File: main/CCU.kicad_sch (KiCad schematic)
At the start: 8 parts, among them U2 ESP32-DevKitC, U27 Oak-D, U4 Waveshare 23721, U5 MPU6050

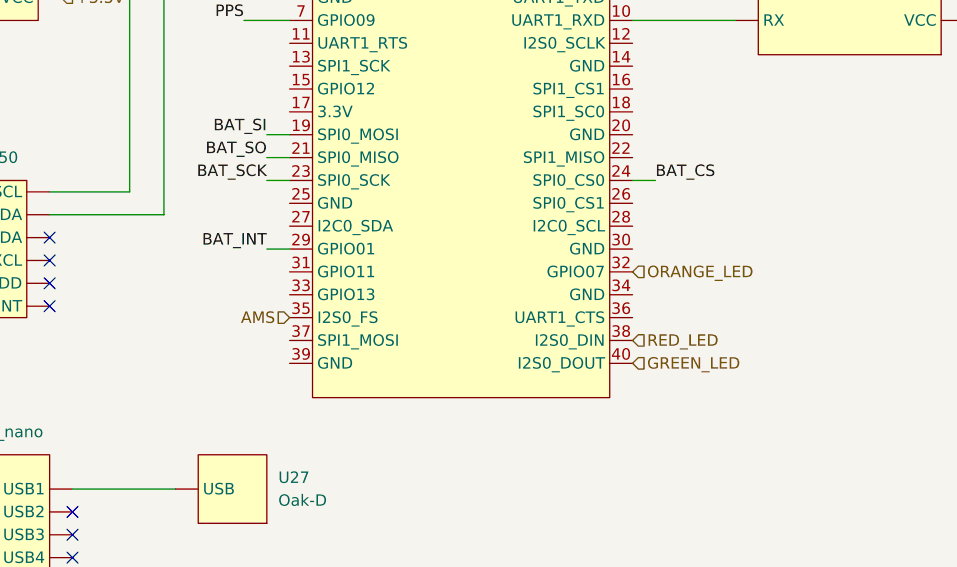
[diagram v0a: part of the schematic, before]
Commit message: added nwe sheet (switching system), created a few new symbols, changed +48V coming from battery to Battery_High_voltage,
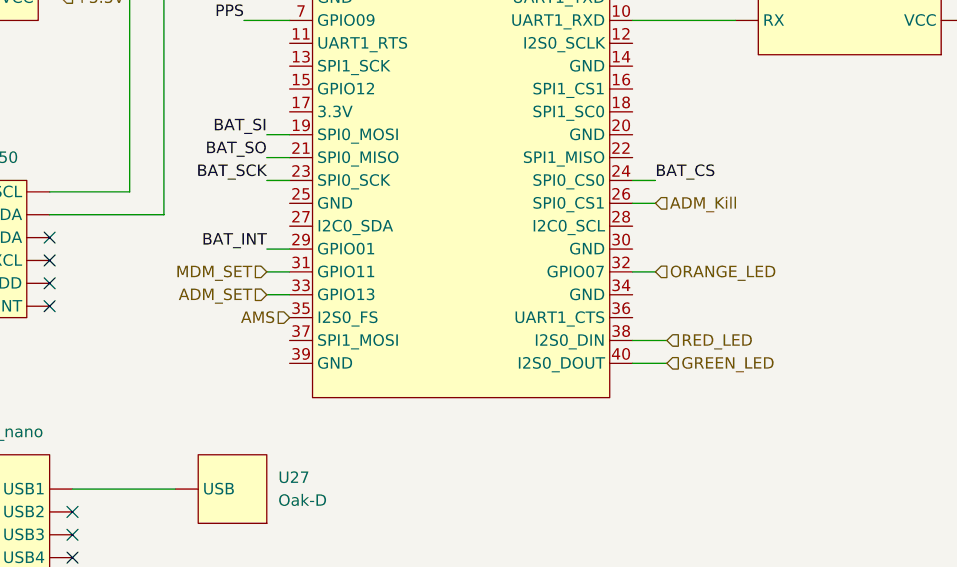
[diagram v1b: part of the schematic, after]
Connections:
- net ADM_Kill: now reaches A4.26 (SPI0_CS1)
- net MDM_SET: now reaches A4.31 (GPIO11)
- net ADM_SET: now reaches A4.33 (GPIO13)
- new net: A22. (VCC), A4.3 (I2C1_SDA), U5. (XDA)
- new net: A22. (VCC), A4.5 (I2C1_SDL), U5. (XDA)
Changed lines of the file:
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@@
+	(wire
+		(pts
+			(xy 194.31 125.73) (xy 190.5 125.73)
+		)
+		(stroke
+			(width 0)
+			(type default)
+		)
+	)
 	(wire
 		(pts
@@
 	(wire
 		(pts
+			(xy 193.04 118.11) (xy 190.5 118.11)
+		)
+		(stroke
+			(width 0)
+			(type default)
+		)
+	)
+	(wire
+		(pts
 			(xy 138.43 82.55) (xy 152.4 82.55)
 		)
@@
 	(wire
 		(pts
+			(xy 190.5 110.49) (xy 193.04 110.49)
+		)
+		(stroke
+			(width 0)
+			(type default)
+		)
+	)
+	(wire
+		(pts
 			(xy 149.86 115.57) (xy 152.4 115.57)
 		)
@@
 	(wire
 		(pts
+			(xy 149.86 120.65) (xy 152.4 120.65)
+		)
+		(stroke
+			(width 0)
+			(type default)
+		)
+	)
+	(wire
+		(pts
 			(xy 147.32 90.17) (xy 152.4 90.17)
 		)
@@
 	(wire
 		(pts
+			(xy 194.31 128.27) (xy 190.5 128.27)
+		)
+		(stroke
+			(width 0)
+			(type default)
+		)
+	)
+	(wire
+		(pts
 			(xy 227.33 86.36) (xy 228.6 86.36)
 		)
@@
 		(pts
 			(xy 124.46 60.96) (xy 127 60.96)
+		)
+		(stroke
+			(width 0)
+			(type default)
+		)
+	)
+	(wire
+		(pts
+			(xy 149.86 118.11) (xy 152.4 118.11)
 		)
 		(stroke
@@
 	(hierarchical_label "RED_LED"
 		(shape input)
-		(at 190.5 125.73 0)
+		(at 194.31 125.73 0)
 		(fields_autoplaced yes)
 		(effects
@@
 	(hierarchical_label "GREEN_LED"
 		(shape input)
-		(at 190.5 128.27 0)
+		(at 194.31 128.27 0)
 		(fields_autoplaced yes)
 		(effects
@@
 	(hierarchical_label "ORANGE_LED"
 		(shape input)
-		(at 190.5 118.11 0)
+		(at 193.04 118.11 0)
 		(fields_autoplaced yes)
 		(effects
@@
 		)
 	)
+	(hierarchical_label "ADM_Kill"
+		(shape input)
+		(at 193.04 110.49 0)
+		(fields_autoplaced yes)
+		(effects
+			(font
+				(size 1.27 1.27)
+			)
+			(justify left)
+		)
+	)
 	(hierarchical_label "+3.3V"
 		(shape input)
@@
 		)
 	)
+	(hierarchical_label "MDM_SET"
+		(shape input)
+		(at 149.86 118.11 180)
+		(fields_autoplaced yes)
+		(effects
+			(font
+				(size 1.27 1.27)
+			)
+			(justify right)
+		)
+	)
 	(hierarchical_label "+3.3V"
 		(shape input)
@@
 		(fields_autoplaced yes)
 		(effects
+			(font
+				(size 1.27 1.27)
+			)
+			(justify right)
+		)
+	)
+	(hierarchical_label "ADM_SET"
+		(shape input)
+		(at 149.86 120.65 180)
+		(fields_autoplaced yes)
+		(effects

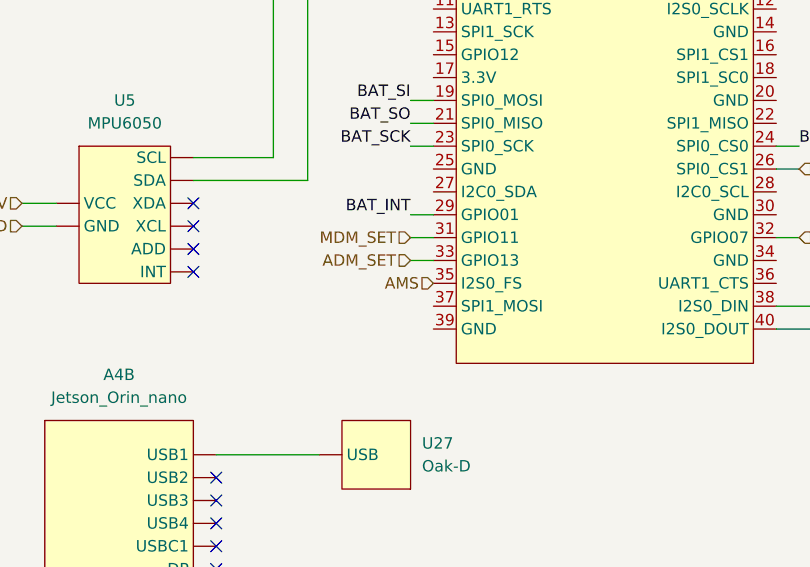
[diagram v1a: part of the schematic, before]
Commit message: removed AMS line, and previous switch ing UI. Renamed Switch in switching system to AMS
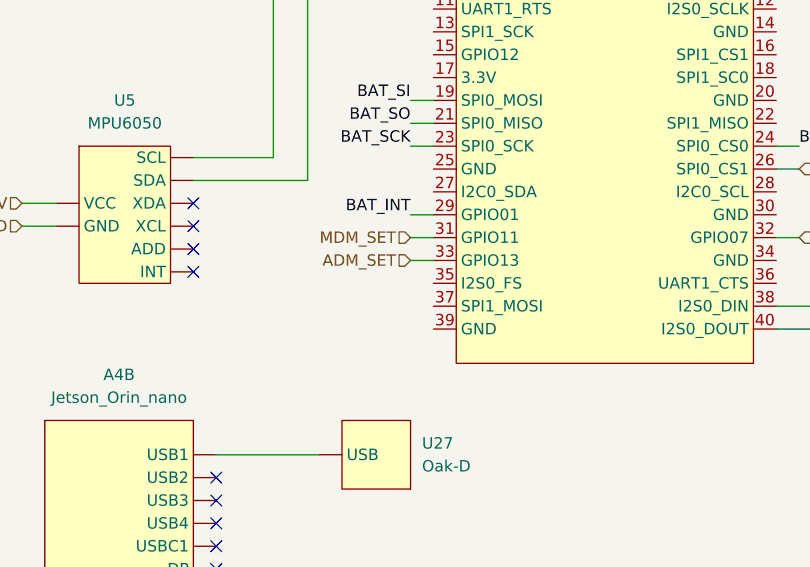
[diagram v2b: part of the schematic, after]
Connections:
- net AMS: no longer names the net of A4.35 (I2S0_FS)
- new net: A22. (VCC), A4.3 (I2C1_SDA), U5. (XDA)
- new net: A22. (VCC), A4.5 (I2C1_SDL), U5. (XDA)
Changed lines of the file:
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@@
-		)
-	)
-	(hierarchical_label "AMS"
-		(shape input)
-		(at 152.4 123.19 180)
-		(fields_autoplaced yes)
-		(effects
-			(font
-				(size 1.27 1.27)
-			)
-			(justify right)
 		)
 	)
